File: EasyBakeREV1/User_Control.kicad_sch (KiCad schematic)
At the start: 12 parts

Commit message: Change main pwr to 3.3 due to USB issues
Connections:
- net VDD renamed VCC
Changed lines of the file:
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@@
   (junction (at 69.85 54.61) (diameter 0) (color 0 0 0 0)
   )
-  (junction (at 72.39 54.61) (diameter 0) (color 0 0 0 0)
-  )
   (junction (at 48.26 24.13) (diameter 0) (color 0 0 0 0)
   )
@@
     (stroke (width 0) (type default))
   )
-  (wire (pts (xy 72.39 54.61) (xy 74.93 54.61))
-    (stroke (width 0) (type default))
-  )
   (wire (pts (xy 48.26 22.86) (xy 48.26 24.13))
     (stroke (width 0) (type default))
@@
     (stroke (width 0) (type default))
   )
+  (wire (pts (xy 69.85 54.61) (xy 74.93 54.61))
+    (stroke (width 0) (type default))
+  )
   (wire (pts (xy 69.85 54.61) (xy 69.85 59.69))
     (stroke (width 0) (type default))
@@
     (stroke (width 0) (type default))
   )
-  (wire (pts (xy 72.39 53.34) (xy 72.39 54.61))
+  (wire (pts (xy 74.93 53.34) (xy 74.93 54.61))
     (stroke (width 0) (type default))
   )
@@
   )
   (wire (pts (xy 57.15 58.42) (xy 54.61 58.42))
-    (stroke (width 0) (type default))
-  )
-  (wire (pts (xy 72.39 54.61) (xy 69.85 54.61))
     (stroke (width 0) (type default))
   )
@@
     (effects (font (size 1.27 1.27) italic) (justify left))
   )
+  (symbol (lib_id "power:VCC") (at 74.93 53.34 0) (unit 1)
+    (in_bom yes) (on_board yes) (dnp no)
+    (property "Reference" "#PWR041" (at 74.93 57.15 0)
+      (effects (font (size 1.27 1.27)) hide)
+    )
+    (property "Value" "VCC" (at 74.93 49.53 0)
+      (effects (font (size 1.27 1.27)))
+    )
+    (property "Footprint" "" (at 74.93 53.34 0)
+      (effects (font (size 1.27 1.27)) hide)
+    )
+    (property "Datasheet" "" (at 74.93 53.34 0)
+      (effects (font (size 1.27 1.27)) hide)
+    )
+    (pin "1")
+    (instances
+      (project "EasyBakeREV1"
+        (path "/e63e39d7-6ac0-4ffd-8aa3-1841a4541b55/562bcfff-999f-4ddd-8529-db8a5890b5a5"
+          (reference "#PWR041") (unit 1)
+        )
+      )
+    )
+  )
   (symbol (lib_id "Device:R_Small_US") (at 64.77 44.45 0) (unit 1)
     (in_bom yes) (on_board yes) (dnp no)
@@
         (path "/e63e39d7-6ac0-4ffd-8aa3-1841a4541b55/562bcfff-999f-4ddd-8529-db8a5890b5a5"
           (reference "R23") (unit 1)
-        )
-      )
-    )
-  )
-  (symbol (lib_id "power:VDD") (at 48.26 22.86 0) (unit 1)
-    (in_bom yes) (on_board yes) (dnp no)
-    (property "Reference" "#PWR041" (at 48.26 26.67 0)
-      (effects (font (size 1.27 1.27)) hide)
-    )
-    (property "Value" "VDD" (at 48.26 19.05 0)
-      (effects (font (size 1.27 1.27)))
-    )
-    (property "Footprint" "" (at 48.26 22.86 0)
-      (effects (font (size 1.27 1.27)) hide)
-    )
-    (property "Datasheet" "" (at 48.26 22.86 0)
-      (effects (font (size 1.27 1.27)) hide)
-    )
-    (pin "1")
-    (instances
-      (project "EasyBakeREV1"
-        (path "/e63e39d7-6ac0-4ffd-8aa3-1841a4541b55/562bcfff-999f-4ddd-8529-db8a5890b5a5"
-          (reference "#PWR041") (unit 1)
         )
       )
@@
   (symbol (lib_id "Switch:SW_SPST") (at 80.01 54.61 0) (unit 1)
     (in_bom yes) (on_board yes) (dnp no)
-    (property "Reference" "SW-M-R1" (at 80.01 49.53 0)
-      (effects (font (size 1.27 1.27)))
-    )
-    (property "Value" "SW_SPST" (at 80.01 50.8 0)
+    (property "Reference" "SW-M-R1" (at 82.55 49.53 0)
+      (effects (font (size 1.27 1.27)))
+    )
+    (property "Value" "SW_SPST" (at 82.55 50.8 0)
       (effects (font (size 1.27 1.27)))
     )
@@
     )
   )
-  (symbol (lib_id "power:VDD") (at 72.39 53.34 0) (unit 1)
-    (in_bom yes) (on_board yes) (dnp no)
-    (property "Reference" "#PWR042" (at 72.39 57.15 0)
-      (effects (font (size 1.27 1.27)) hide)
-    )
-    (property "Value" "VDD" (at 72.39 49.53 0)
-      (effects (font (size 1.27 1.27)))
-    )
-    (property "Footprint" "" (at 72.39 53.34 0)
-      (effects (font (size 1.27 1.27)) hide)
-    )
-    (property "Datasheet" "" (at 72.39 53.34 0)
+  (symbol (lib_id "Switch:SW_SPST") (at 69.85 44.45 90) (unit 1)
+    (in_bom yes) (on_board yes) (dnp no)
+    (property "Reference" "SW-M-UP1" (at 71.12 43.1799 90)
+      (effects (font (size 1.27 1.27)) (justify right))
+    )
+    (property "Value" "SW_SPST" (at 71.12 44.45 90)
+      (effects (font (size 1.27 1.27)) (justify right))
+    )
+    (property "Footprint" "Daxxn_Switches:TL3365AF180QG" (at 69.85 44.45 0)
+      (effects (font (size 1.27 1.27)) hide)
+    )
+    (property "Datasheet" "~" (at 69.85 44.45 0)
+      (effects (font (size 1.27 1.27)) hide)
+    )
+    (pin "1")
+    (pin "2")
+    (instances
+      (project "EasyBakeREV1"
+        (path "/e63e39d7-6ac0-4ffd-8aa3-1841a4541b55/562bcfff-999f-4ddd-8529-db8a5890b5a5"
+          (reference "SW-M-UP1") (unit 1)
+        )
+      )
+    )
+  )
+  (symbol (lib_id "power:VCC") (at 48.26 22.86 0) (unit 1)
+    (in_bom yes) (on_board yes) (dnp no)
+    (property "Reference" "#PWR042" (at 48.26 26.67 0)
+      (effects (font (size 1.27 1.27)) hide)
+    )
+    (property "Value" "VCC" (at 48.26 19.05 0)
+      (effects (font (size 1.27 1.27)))
+    )
+    (property "Footprint" "" (at 48.26 22.86 0)
+      (effects (font (size 1.27 1.27)) hide)
+    )
+    (property "Datasheet" "" (at 48.26 22.86 0)
       (effects (font (size 1.27 1.27)) hide)
     )
@@
         )
       )
-    )
-  )
-  (symbol (lib_id "Switch:SW_SPST") (at 69.85 44.45 90) (unit 1)
-    (in_bom yes) (on_board yes) (dnp no)
-    (property "Reference" "SW-M-UP1" (at 71.12 43.1799 90)
-      (effects (font (size 1.27 1.27)) (justify right))
-    )
-    (property "Value" "SW_SPST" (at 71.12 44.45 90)
-      (effects (font (size 1.27 1.27)) (justify right))
-    )
-    (property "Footprint" "Daxxn_Switches:TL3365AF180QG" (at 69.85 44.45 0)
-      (effects (font (size 1.27 1.27)) hide)
-    )
-    (property "Datasheet" "~" (at 69.85 44.45 0)
-      (effects (font (size 1.27 1.27)) hide)
-    )
-    (pin "1")
-    (pin "2")
-    (instances
-      (project "EasyBakeREV1"
-        (path "/e63e39d7-6ac0-4ffd-8aa3-1841a4541b55/562bcfff-999f-4ddd-8529-db8a5890b5a5"
-          (reference "SW-M-UP1") (unit 1)
-        )
-      )

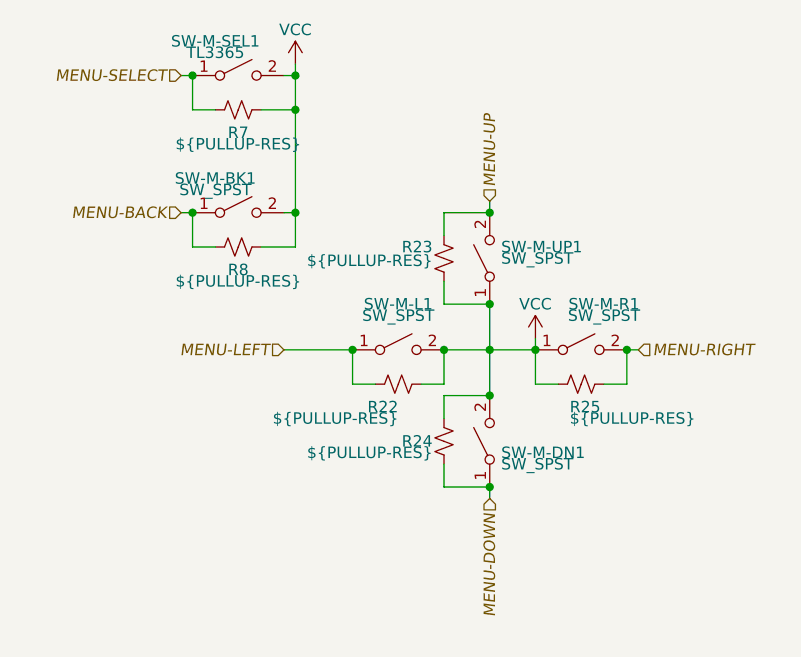
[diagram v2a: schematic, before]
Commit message: Replaced MCU - started layout
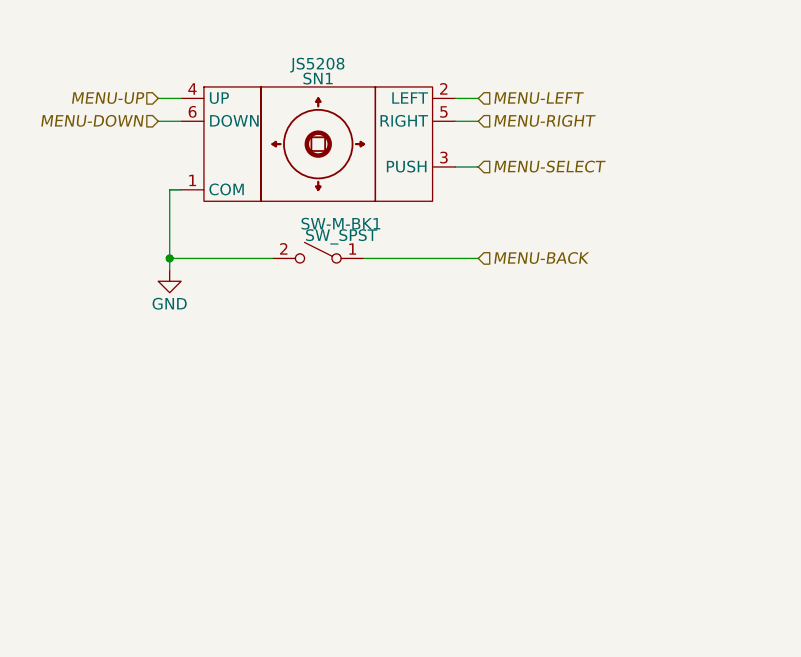
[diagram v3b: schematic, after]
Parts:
- removed R22, R23, R24, R25, R7, R8: ${PULLUP-RES}, Resistor_SMD:R_0805_2012Metric, symbol Device:R_Small_US
- removed SW-M-DN1, SW-M-L1, SW-M-R1, SW-M-UP1: SW_SPST, Daxxn_Switches:TL3365AF180QG, symbol Switch:SW_SPST
- removed SW-M-SEL1: TL3365, Daxxn_Switches:TL3365AF180QG, symbol Switch:SW_SPST
- added SN1: JS5208, Daxxn_Switches:JS5208, symbol Daxxn_Buttons:JS5208
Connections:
- net MENU-DOWN: now also SN1.6 (DOWN)
- net MENU-LEFT: now also SN1.2 (LEFT)
- net MENU-RIGHT: now also SN1.5 (RIGHT)
- net MENU-SELECT: now also SN1.3 (PUSH)
- net MENU-UP: now also SN1.4 (UP)
- net VCC renamed GND
- net GND: now also SN1.1 (COM)
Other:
- moved on the sheet: SW-M-BK1
